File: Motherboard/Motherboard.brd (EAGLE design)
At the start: 87.5 x 150 mm, 13 parts

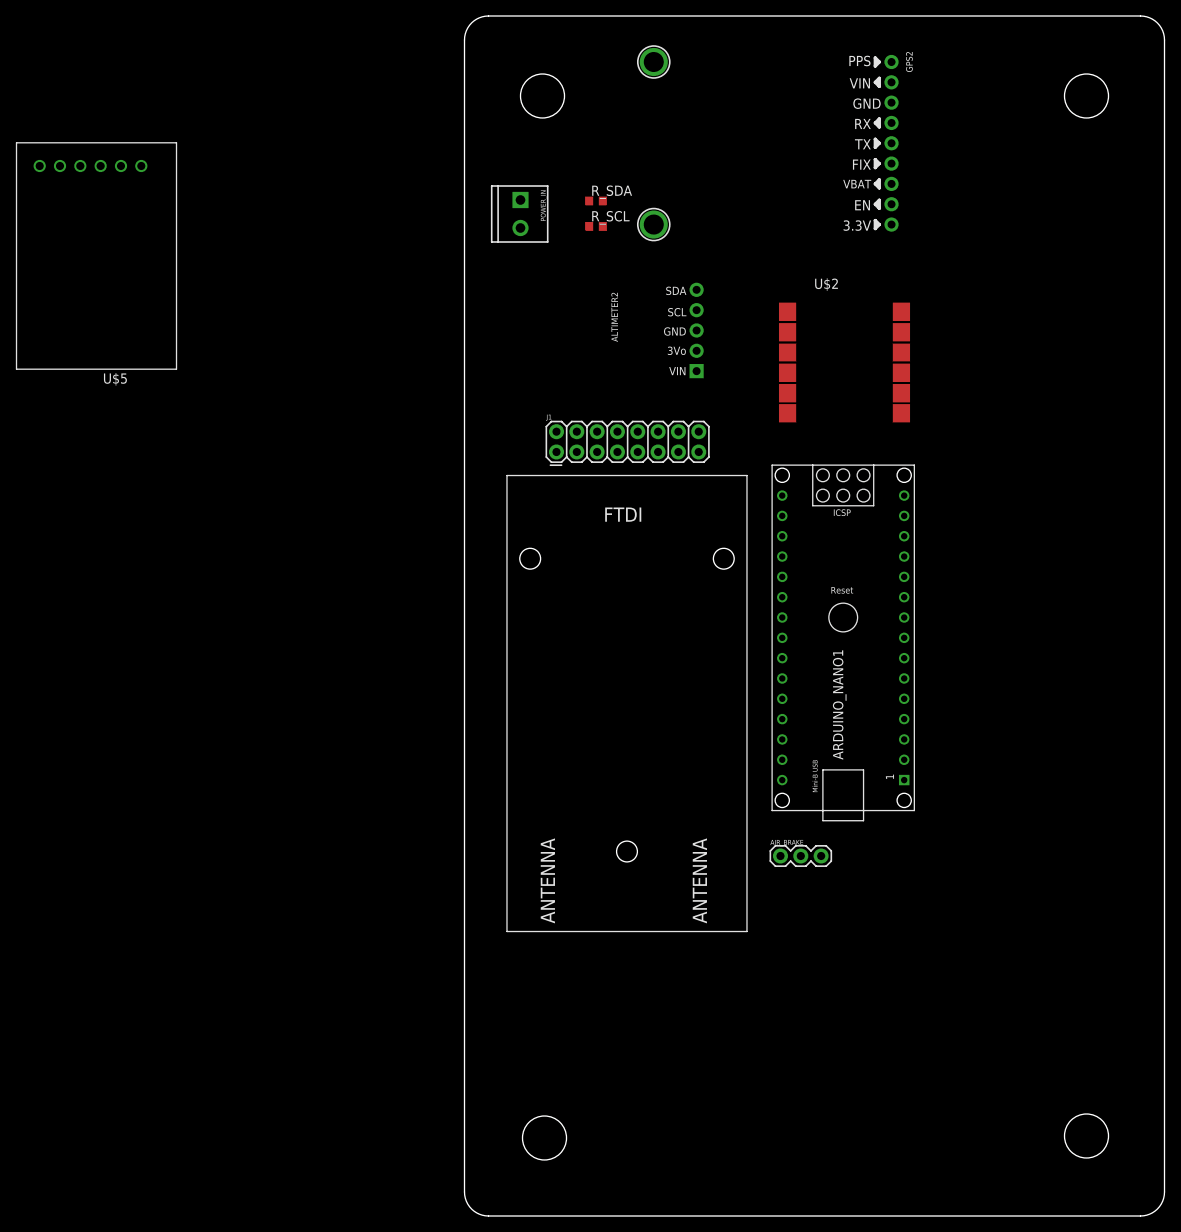
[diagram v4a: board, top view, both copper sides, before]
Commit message: add components to boards
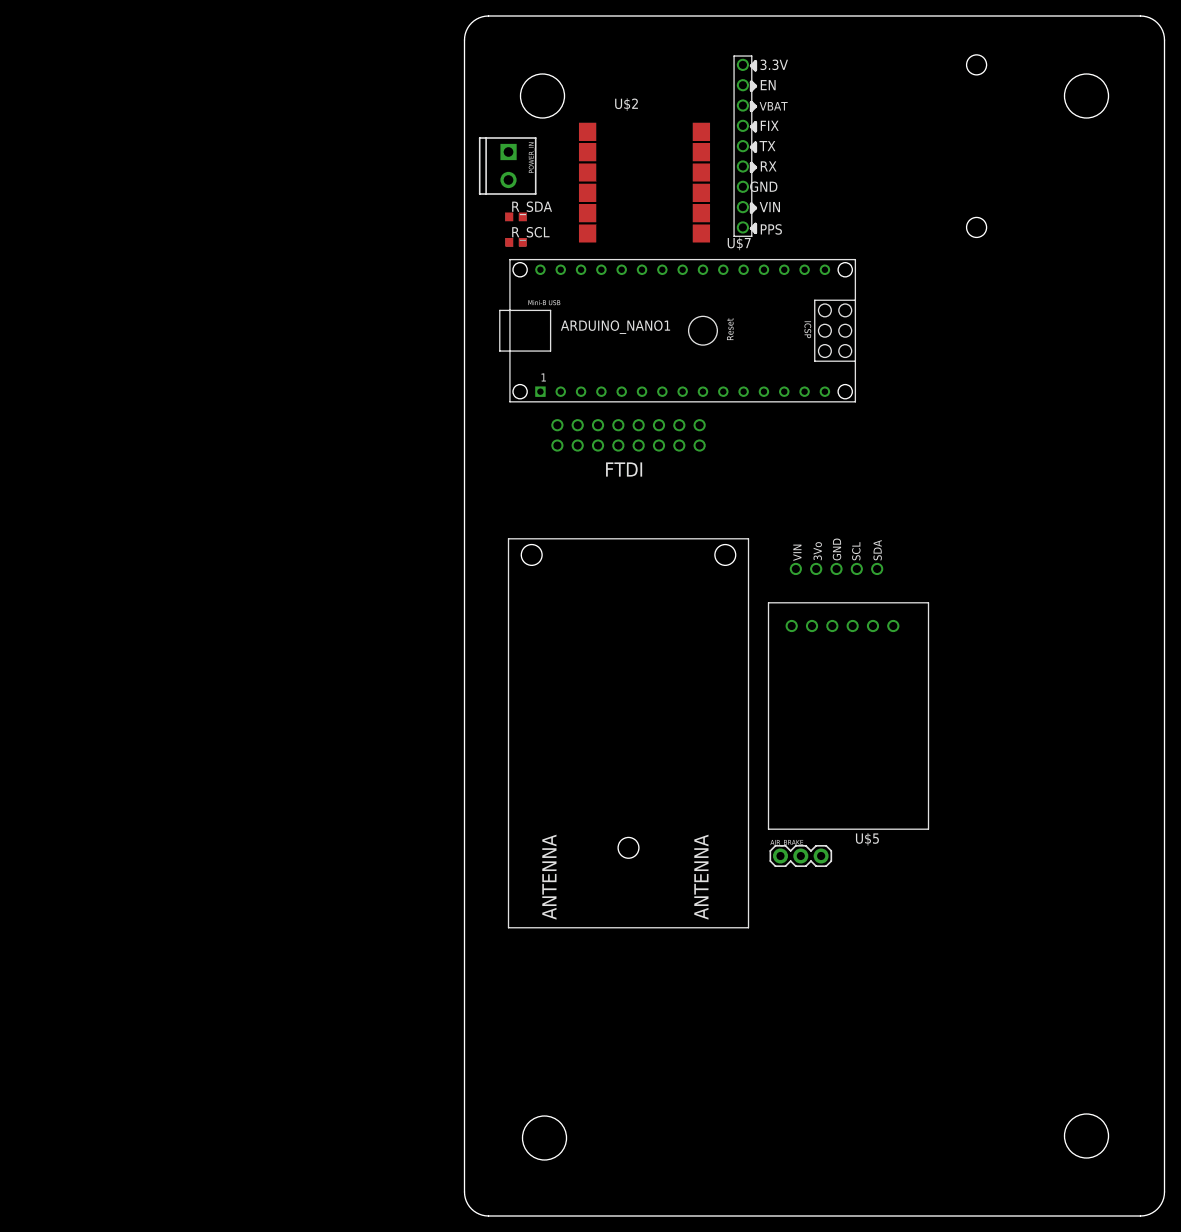
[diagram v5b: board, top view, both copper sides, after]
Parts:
- removed ALTIMETER2: (no value), microbuilder:1X05_ROUND_70
- removed GPS2: (no value), microbuilder:1X09_ROUND_70
- removed J1: (no value), SparkFun-Connectors:2X8
- removed U$3, U$4: MOUNTINGHOLE2.5, microbuilder:MOUNTINGHOLE_2.5_PLATED
- added U$6: RADIO, uORocketry-parts:RADIO
- added U$7: GPS, uORocketry-parts:GPS
- U$1: value (none) -> ALTIMETER; device ArduinoNanoV30:RADIO -> uORocketry-parts:ALTIMETER
- moved U$5 110.2 mm to (48.0, 62.5)
- moved ARDUINO_NANO1 39.9 mm to (29.8, 110.7), turned to 0 degrees
- moved U$1 36.3 mm to (46.5, 88.5), turned to 270 degrees
- moved U$2 33.6 mm to (22.5, 129.5)
- moved R_SCL 10.2 mm to (6.44, 121.7)
- moved R_SDA 10.2 mm to (6.44, 124.9)
- moved POWER_IN 6.18 mm to (5.50, 133.0)
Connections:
- new net MISO: ARDUINO_NANO1.30, U$5.MISO
- new net MOSI: ARDUINO_NANO1.29, U$5.MOSI
- new net SCK: ARDUINO_NANO1.1, U$5.SCK
- new net SS: ARDUINO_NANO1.28, U$5.SS
- net +5V: no longer J1.6
- net 3V3: now also U$1.VIN; no longer ALTIMETER2.1, GPS2.1
- net 5V: now also U$6.5VUSB2
- net GND: now also U$1.GND, U$6.GND_1, U$7.GND; no longer ALTIMETER2.3, GPS2.7, J1.2
- net RADIO_SHORT: now also U$6.5V, U$6.5VUSB; no longer J1.3, J1.5
- net RX: now also U$7.TX; no longer GPS2.5
- net RX0: now also U$6.SITX; no longer J1.10
- net SCL: now also U$1.SCL; no longer ALTIMETER2.4
- net SDA: now also U$1.SDA; no longer ALTIMETER2.5
- net TX: now also U$7.RX; no longer GPS2.6
- net TX1: now also U$6.SIRX; no longer J1.8
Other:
- board text removed: "3.3V"
- board text removed: "3Vo"
- board text removed: "EN"
- board text removed: "FIX"
- board text removed: "GND"
- board text removed: "PPS"
- board text removed: "RX"
- board text removed: "SCL"
- board text removed: "SDA"
- board text removed: "TX"
- board text removed: "VBAT"
- board text removed: "VIN"

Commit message: more layout
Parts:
- added U$3: RS232, uORocketry-parts:RS232
- moved U$2 24.2 mm to (10.5, 108.5)
- moved U$7 24.2 mm to (37.5, 112.0), turned to 0 degrees
- moved AIR_BRAKE 23.0 mm to (38.5, 22.0)
- moved U$6 22.0 mm to (19.0, 24.0)
- moved ARDUINO_NANO1 22.0 mm to (29.8, 88.7)
- moved U$1 21.1 mm to (44.5, 67.5)
- moved U$5 19.2 mm to (45.0, 43.5)
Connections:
- new net SBG_RX: ARDUINO_NANO1.23, U$3.RX-1
- new net SBG_TX: ARDUINO_NANO1.22, U$3.TX-0
- net 5V: now also U$3.VCC
- net GND: now also U$3.GND
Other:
- outline, holes or cut-outs redrawn

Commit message: routing
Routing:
- net GND: track 0.00 -> 228.9 mm, vias 0 -> 1
- net +5V: track 0.00 -> 177.2 mm
- net 5V: track 0.00 -> 153.9 mm, vias 0 -> 1
- net N$4: track 0.00 -> 122.4 mm
- net SDA: track 0.00 -> 99.8 mm, vias 0 -> 2
- net SCL: track 0.00 -> 99.4 mm, vias 0 -> 1
- net 3V3: track 0.00 -> 95.2 mm
- net SS: track 0.00 -> 84.0 mm, vias 0 -> 1
- net MISO: track 0.00 -> 77.4 mm, vias 0 -> 1
- net MOSI: track 0.00 -> 68.5 mm
- net SCK: track 0.00 -> 56.6 mm
- net TX1: track 0.00 -> 52.6 mm, vias 0 -> 1
- net SBG_RX: track 0.00 -> 35.4 mm
- net SBG_TX: track 0.00 -> 35.0 mm
- net RX: track 0.00 -> 26.1 mm
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
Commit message: more routing
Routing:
- net RX0: track 0.00 -> 38.3 mm, vias 0 -> 1
- net 5V: track 153.9 -> 122.9 mm, vias 1 -> 0
- net MOSI: track 68.5 -> 88.8 mm
- net SBG_TX: track 35.0 -> 54.1 mm
- net 3V3: track 95.2 -> 113.0 mm, vias 0 -> 2
- net MISO: track 77.4 -> 94.0 mm, vias 1 -> 0
- net SDA: track 99.8 -> 113.1 mm
- net TX1: track 52.6 -> 40.1 mm, vias 1 -> 2
- net +5V: track 177.2 -> 165.3 mm
- net SBG_RX: track 35.4 -> 44.4 mm
- net N$4: track 122.4 -> 128.4 mm
- net SCL: track 99.4 -> 104.3 mm
- net GND: track 228.9 -> 224.1 mm, vias 1 -> 0
- net SS: track 84.0 -> 86.4 mm, vias 1 -> 0
- net TX: track 24.7 -> 25.8 mm, vias 0 -> 1
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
